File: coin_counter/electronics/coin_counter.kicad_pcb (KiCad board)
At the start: 2 copper layers, 185.3 x 82 mm, 54 parts, among them J1 Q_EMT, J10 H_EMT, J11 Power In, J12 Q_BTN, J13 D_BTN, J14 N_BTN, J15 P_BTN, J16 UP_BTN, J17 DN_BTN, J18 VFD, J19 i/o in, J2 N_EMT, J20 i/o in, J21 Power In, J22 Power Out, J23 i/o out, J24 i/o out, J25 H_RCV, J3 P_EMT, J4 D_EMT, J5 Mom, J6 D_RCV, J7 P_RCV, J8 N_RCV, J9 Q_RCV, U1 74HC595, U2 74HC165, U3 74HC165

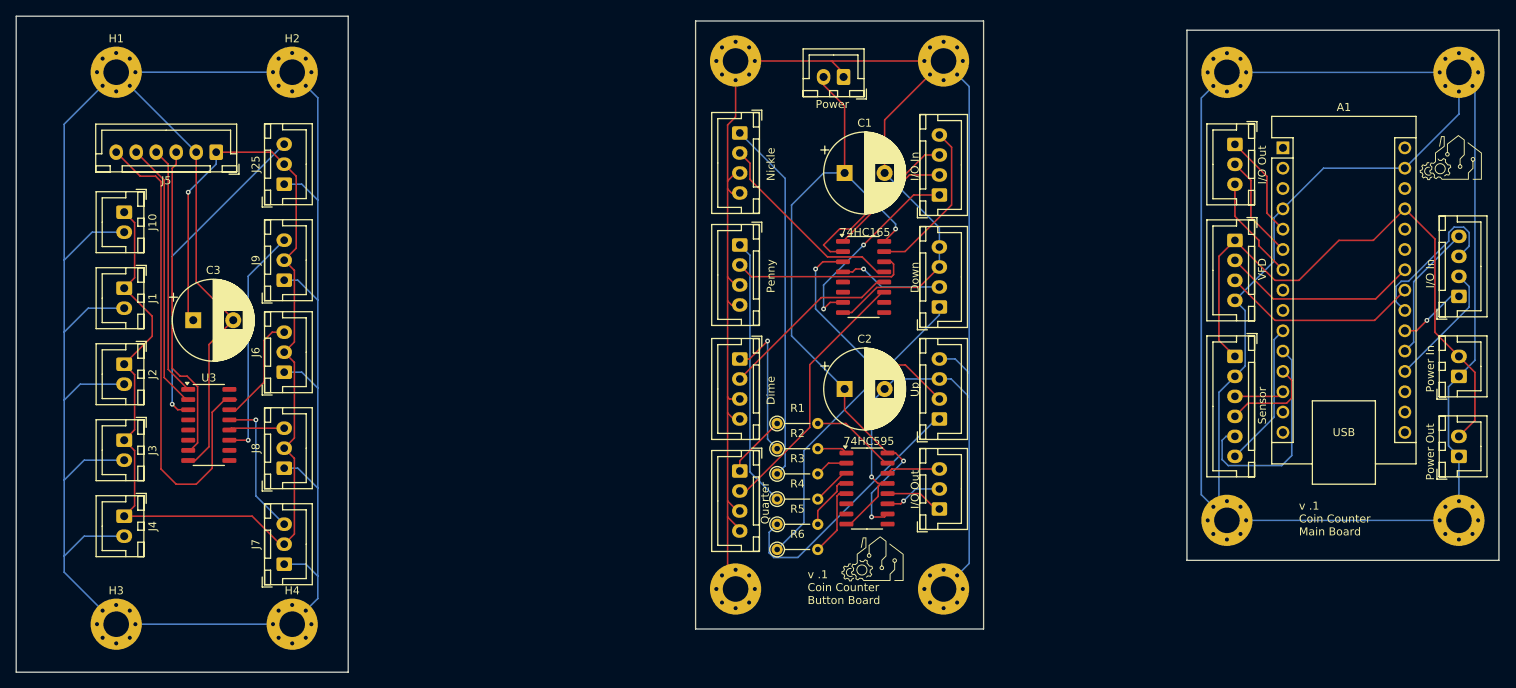
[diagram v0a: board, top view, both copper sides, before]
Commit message: more work, mosfets and diodes
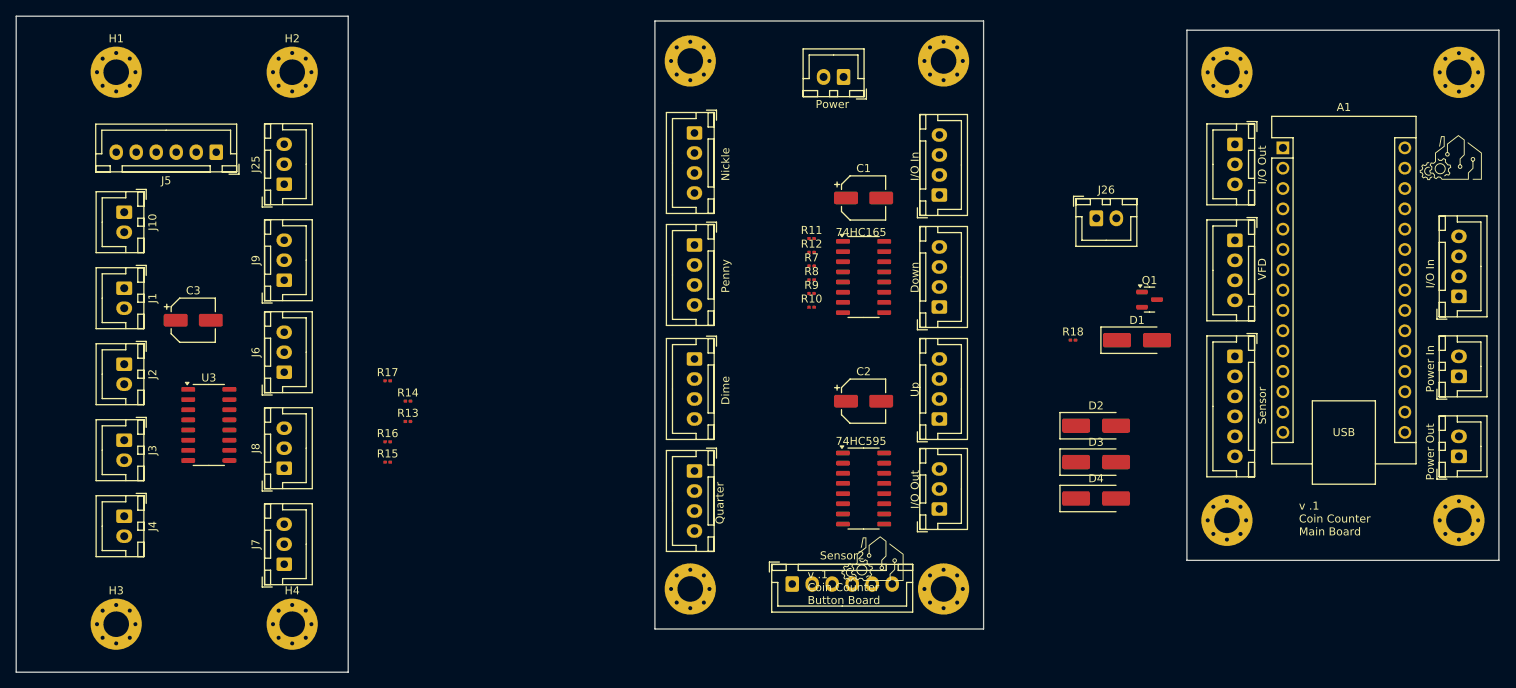
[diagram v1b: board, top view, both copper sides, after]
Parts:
- removed R1, R2, R3, R4, R5, R6: 220 Ohm, Resistor_THT:R_Axial_DIN0204_L3.6mm_D1.6mm_P5.08mm_Vertical
- added D1: D_Schottky, Diode_SMD:D_SMA_Handsoldering, F.Cu at (162.6, 63.5)
- added D2: D_Schottky, Diode_SMD:D_SMA_Handsoldering, F.Cu at (157.5, 74.2)
- added D3: D_Schottky, Diode_SMD:D_SMA_Handsoldering, F.Cu at (157.5, 78.7)
- added D4: D_Schottky, Diode_SMD:D_SMA_Handsoldering, F.Cu at (157.5, 83.3)
- added J26: Motor, Connector_JST:JST_XH_B2B-XH-A_1x02_P2.50mm_Vertical, F.Cu at (157.5, 48.3)
- added Q1: DMN6075S, Package_TO_SOT_SMD:SOT-23, F.Cu at (164.2, 58.4)
- added R10: 10k, Resistor_SMD:R_0201_0603Metric, F.Cu at (121.9, 59.4)
- added R11: 10k, Resistor_SMD:R_0201_0603Metric, F.Cu at (121.9, 50.8)
- added R12: 10k, Resistor_SMD:R_0201_0603Metric, F.Cu at (121.9, 52.5)
- added R13: 10k, Resistor_SMD:R_0201_0603Metric, F.Cu at (71.5, 73.7)
- added R14: 10k, Resistor_SMD:R_0201_0603Metric, F.Cu at (71.5, 71.1)
- added R15: 10k, Resistor_SMD:R_0201_0603Metric, F.Cu at (68.9, 78.7)
- added R16: 10k, Resistor_SMD:R_0201_0603Metric, F.Cu at (68.9, 76.2)
- added R17: 10k, Resistor_SMD:R_0201_0603Metric, F.Cu at (68.9, 68.6)
- added R18: 10k, Resistor_SMD:R_0201_0603Metric, F.Cu at (154.6, 63.5)
- added R7: 10k, Resistor_SMD:R_0201_0603Metric, F.Cu at (121.9, 54.2)
- added R8: 10k, Resistor_SMD:R_0201_0603Metric, F.Cu at (121.9, 55.9)
- added R9: 10k, Resistor_SMD:R_0201_0603Metric, F.Cu at (121.9, 57.7)
- added Sensor2: Mom, Connector_JST:JST_XH_B6B-XH-A_1x06_P2.50mm_Vertical, F.Cu at (119.5, 94.0)
- C1, C2, C3: footprint Capacitor_THT:CP_Radial_D10.0mm_P5.00mm -> Capacitor_SMD:CP_Elec_5x5.9
- moved J12 5.66 mm to (107.3, 79.8)
- moved J13 5.66 mm to (107.3, 65.8)
- moved J14 5.66 mm to (107.3, 37.6)
- moved J15 5.66 mm to (107.3, 51.6)
- moved H11 5.66 mm to (106.8, 28.6)
- moved H12 5.66 mm to (106.8, 94.6)
- moved C1 3.92 mm to (128.4, 45.7)
- moved C2 2.81 mm to (128.4, 71.1)
- moved U1 0.42 mm to (128.4, 82.0)
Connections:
- A1 pad 10: Net-(A1-D7) -> unconnected-(A1-D7-Pad10)
- A1 pad 11: Net-(A1-D8) -> unconnected-(A1-D8-Pad11)
- A1 pad 12: Net-(A1-D9) -> unconnected-(A1-D9-Pad12)
- A1 pad 13: Net-(A1-D10) -> unconnected-(A1-D10-Pad13)
- A1 pad 29: Net-(J11-Pin_1) -> Net-(D4-A)
- A1 pad 4: Net-(J11-Pin_1) -> Net-(D4-A)
- A1 pad 9: unconnected-(A1-D6-Pad9) -> Net-(A1-D6)
- C1 pad 1: Net-(J21-Pin_2) -> Net-(J12-Pin_3)
- C1 pad 2: Net-(J12-Pin_3) -> Net-(J12-Pin_4)
- C2 pad 1: Net-(J21-Pin_2) -> Net-(J12-Pin_3)
- C2 pad 2: Net-(J12-Pin_3) -> Net-(J12-Pin_4)
- H10 pad 1: Net-(J12-Pin_3) -> Net-(J12-Pin_4)
- H11 pad 1: Net-(J12-Pin_3) -> Net-(J12-Pin_4)
- H12 pad 1: Net-(J12-Pin_3) -> Net-(J12-Pin_4)
- H5 pad 1: Net-(J11-Pin_1) -> Net-(D4-A)
- H6 pad 1: Net-(J11-Pin_1) -> Net-(D4-A)
- H7 pad 1: Net-(J11-Pin_1) -> Net-(D4-A)
- H8 pad 1: Net-(J11-Pin_1) -> Net-(D4-A)
- H9 pad 1: Net-(J12-Pin_3) -> Net-(J12-Pin_4)
- J12 pad 4: Net-(J12-Pin_3) -> Net-(J12-Pin_4)
- J13 pad 4: Net-(J12-Pin_3) -> Net-(J12-Pin_4)
- J14 pad 4: Net-(J12-Pin_3) -> Net-(J12-Pin_4)
- J15 pad 4: Net-(J12-Pin_3) -> Net-(J12-Pin_4)
- J16 pad 4: Net-(J12-Pin_3) -> Net-(J12-Pin_4)
- J17 pad 4: Net-(J12-Pin_3) -> Net-(J12-Pin_4)
- J18 pad 4: Net-(J11-Pin_1) -> Net-(D4-A)
- J21 pad 1: Net-(J12-Pin_3) -> Net-(J12-Pin_4)
- J21 pad 2: Net-(J21-Pin_2) -> Net-(J12-Pin_3)
- U1 pad 1: Net-(U1-QB) -> Net-(J13-Pin_1)
- U1 pad 10: Net-(J21-Pin_2) -> Net-(J12-Pin_3)
- U1 pad 13: Net-(J12-Pin_3) -> Net-(J12-Pin_4)
- U1 pad 15: Net-(U1-QA) -> Net-(J12-Pin_1)
- U1 pad 16: Net-(J21-Pin_2) -> Net-(J12-Pin_3)
- U1 pad 2: Net-(U1-QC) -> Net-(J14-Pin_1)
- U1 pad 3: Net-(U1-QD) -> Net-(J15-Pin_1)
- U1 pad 4: Net-(U1-QE) -> Net-(J16-Pin_1)
- U1 pad 5: Net-(U1-QF) -> Net-(J17-Pin_1)
- U1 pad 8: Net-(J12-Pin_3) -> Net-(J12-Pin_4)
- U2 pad 10: unconnected-(U2-DS-Pad10) -> Net-(Sensor2-Pin_3)
- U2 pad 11: Net-(J12-Pin_2) -> Net-(U2-D0)
- U2 pad 12: Net-(J13-Pin_2) -> Net-(U2-D1)
- U2 pad 13: Net-(J14-Pin_2) -> Net-(U2-D2)
- U2 pad 14: Net-(J15-Pin_2) -> Net-(U2-D3)
- U2 pad 16: Net-(J21-Pin_2) -> Net-(J12-Pin_3)
- U2 pad 3: Net-(J16-Pin_2) -> Net-(U2-D4)
- U2 pad 4: Net-(J17-Pin_2) -> Net-(U2-D5)
- U2 pad 5: unconnected-(U2-D6-Pad5) -> Net-(J12-Pin_4)
- U2 pad 6: unconnected-(U2-D7-Pad6) -> Net-(J12-Pin_4)
- U2 pad 7: Net-(J19-Pin_1) -> unconnected-(U2-~{Q7}-Pad7)
- U2 pad 8: Net-(J12-Pin_3) -> Net-(J12-Pin_4)
- U2 pad 9: unconnected-(U2-Q7-Pad9) -> Net-(J19-Pin_1)
- U3 pad 11: Net-(J9-Pin_3) -> Net-(U3-D0)
- U3 pad 12: Net-(J8-Pin_3) -> Net-(U3-D1)
- U3 pad 13: Net-(J7-Pin_3) -> Net-(U3-D2)
- U3 pad 14: Net-(J6-Pin_3) -> Net-(U3-D3)
- U3 pad 3: Net-(J25-Pin_3) -> Net-(U3-D4)
- U3 pad 7: Net-(J5-Pin_3) -> unconnected-(U3-~{Q7}-Pad7)
- U3 pad 9: unconnected-(U3-Q7-Pad9) -> Net-(J5-Pin_3)
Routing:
- net GND: track 315.9 -> 0.00 mm
- net Net-(J12-Pin_3): track 266.8 -> 0.00 mm, vias 1 -> 0
- net Net-(J11-Pin_1): track 251.2 -> 0.00 mm
- net +5V: track 149.3 -> 0.00 mm, vias 1 -> 0
- net Net-(J21-Pin_2): track 82.4 -> 0.00 mm, vias 3 -> 0
- net Net-(A1-+5V): track 76.1 -> 0.00 mm
- net Net-(J5-Pin_6): track 61.7 -> 0.00 mm
- net Net-(J14-Pin_1): track 45.4 -> 0.00 mm
- net Net-(J25-Pin_3): track 40.6 -> 0.00 mm, vias 1 -> 0
- net Net-(J5-Pin_3): track 39.9 -> 0.00 mm
- net Net-(J17-Pin_1): track 38.7 -> 0.00 mm
- net Net-(J5-Pin_5): track 33.8 -> 0.00 mm
- net Net-(J15-Pin_1): track 33.7 -> 0.00 mm
- net Net-(J12-Pin_2): track 32.9 -> 0.00 mm
- net Net-(J16-Pin_1): track 32.7 -> 0.00 mm
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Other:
- outline, holes or cut-outs redrawn

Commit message: board layouts button and main
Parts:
- removed Sensor: Board, PCM_kikit:Board
- removed Sensor1: Mom, Connector_JST:JST_XH_B6B-XH-A_1x06_P2.50mm_Vertical
- moved D2 47.4 mm to (192.0, 41.8)
- moved D3 46.9 mm to (192.0, 47.0), turned to 180 degrees
- moved D1 39.9 mm to (192.0, 36.5), turned to 180 degrees
- moved D4 38.1 mm to (174.0, 49.0)
- moved R7 31.1 mm to (114.7, 84.5), turned to 180 degrees
- moved J18 31.0 mm to (174.5, 82.0)
- moved J23 31.0 mm to (174.5, 70.0)
- moved R18 30.6 mm to (180.3, 47.0), turned to -90 degrees
- moved J26 20.8 mm to (174.5, 60.2), turned to -90 degrees
- moved R11 20.2 mm to (129.7, 69.5)
- moved R12 16.9 mm to (129.7, 67.5)
- moved R8 16.7 mm to (114.7, 71.0), turned to 180 degrees
- moved A1 15.0 mm to (180.8, 54.5)
- moved R9 13.7 mm to (114.7, 46.0), turned to 180 degrees
- moved H8 12.0 mm to (203.4, 98.0)
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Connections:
- A1 pad 29: Net-(D4-A) -> Net-(J11-Pin_1)
- A1 pad 4: Net-(D4-A) -> Net-(J11-Pin_1)
- D3 pad 1: Net-(D3-K) -> Net-(A1-+5V)
- H5 pad 1: Net-(D4-A) -> Net-(J11-Pin_1)
- H6 pad 1: Net-(D4-A) -> Net-(J11-Pin_1)
- H7 pad 1: Net-(D4-A) -> Net-(J11-Pin_1)
- H8 pad 1: Net-(D4-A) -> Net-(J11-Pin_1)
- J18 pad 4: Net-(D4-A) -> Net-(J11-Pin_1)
- Q1 pad 2: Net-(D4-A) -> Net-(J11-Pin_1)
- Q1 pad 3: Net-(D3-K) -> Net-(D4-A)
- R18 pad 2: Net-(D4-A) -> Net-(J11-Pin_1)
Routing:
- net Net-(J12-Pin_4): track 0.00 -> 298.1 mm
- net Net-(J11-Pin_1): track 0.00 -> 212.4 mm, vias 0 -> 2
- net Net-(J12-Pin_3): track 0.00 -> 169.1 mm, vias 0 -> 5
- net Net-(A1-+5V): track 0.00 -> 120.5 mm
- net Net-(J19-Pin_3): track 0.00 -> 87.6 mm, vias 0 -> 2
- net Net-(J19-Pin_2): track 0.00 -> 82.6 mm, vias 0 -> 3
- net Net-(J19-Pin_4): track 0.00 -> 78.7 mm, vias 0 -> 2
- net Net-(A1-D6): track 0.00 -> 53.8 mm, vias 0 -> 1
- net Net-(A1-SCL/A5): track 0.00 -> 50.1 mm
- net Net-(J14-Pin_1): track 0.00 -> 48.6 mm
- net Net-(Sensor2-Pin_3): track 0.00 -> 47.7 mm, vias 0 -> 1
- net Net-(A1-SDA/A4): track 0.00 -> 46.3 mm
- net Net-(D1-A): track 0.00 -> 40.2 mm
- net Net-(J15-Pin_1): track 0.00 -> 39.0 mm
- net Net-(J17-Pin_1): track 0.00 -> 34.7 mm, vias 0 -> 1
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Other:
- board size 185.3 x 82 mm -> 185.5 x 82 mm
- board text added: "Motor"
- board text added: "v .2 Coin Counter Button Board"
- board text added: "v .2 Coin Counter Main Board"
- board text removed: "Sensor"
- board text removed: "v .1 Coin Counter Button Board"
- board text removed: "v .1 Coin Counter Main Board"

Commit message: v2 of boards
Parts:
- added Sensor_2: Board, PCM_kikit:Board, F.Cu at (44.0, 25.5)
- moved H5 56.4 mm to (118.7, 28.6)
- moved A1 56.4 mm to (125.3, 44.6)
- moved D1 56.4 mm to (136.5, 26.6)
- moved D2 56.4 mm to (136.5, 31.9)
- moved D3 56.4 mm to (136.5, 37.1)
- moved D4 56.4 mm to (118.5, 39.1)
- moved H7 56.4 mm to (148.5, 28.6)
- moved J20 56.4 mm to (146.5, 59.6)
- moved J23 56.4 mm to (119.0, 60.1)
- moved J26 56.4 mm to (119.0, 50.4)
- moved Main 56.4 mm to (121.5, 23.1)
- moved Q1 56.4 mm to (118.5, 44.1)
- moved R18 56.4 mm to (124.8, 37.1)
- moved H8 56.4 mm to (147.9, 88.2)
- moved J11 56.4 mm to (146.5, 69.7)
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- renumbered U3 to 74HC165, J4 to D_EMT, J6 to D_RECV, J10 to H_EMT, J25 to H_RECV, J2 to N_EMT, J8 to N_RECV, J3 to P_EMT, J7 to P_RECV, J9 to Q_RECV, J5 to Sensor
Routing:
- net GND: track 0.00 -> 282.2 mm
- net +5V: track 0.00 -> 173.6 mm, vias 0 -> 2
- net Net-(J5-Pin_6): track 0.00 -> 54.7 mm, vias 0 -> 1
- net Net-(J5-Pin_4): track 0.00 -> 47.0 mm, vias 0 -> 2
- net Net-(J5-Pin_5): track 0.00 -> 42.2 mm, vias 0 -> 1
- net Net-(J5-Pin_3): track 0.00 -> 40.0 mm, vias 0 -> 2
- net Net-(U3-D4): track 0.00 -> 36.1 mm
- net Net-(U3-D0): track 0.00 -> 35.6 mm
- net Net-(U3-D3): track 0.00 -> 20.6 mm
- net Net-(U3-D1): track 0.00 -> 16.7 mm, vias 0 -> 2
- net Net-(U3-D2): track 0.00 -> 10.1 mm
- net Net-(J8-Pin_3): track 0.00 -> 6.67 mm
- net Net-(J9-Pin_3): track 0.00 -> 4.02 mm
- net Net-(J7-Pin_3): track 0.00 -> 4.02 mm
- net Net-(J25-Pin_3): track 0.00 -> 4.02 mm
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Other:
- board size 185.5 x 82 mm -> 122.5 x 80.3 mm
- board text added: "v .2 Coin Counter Sensor Board"

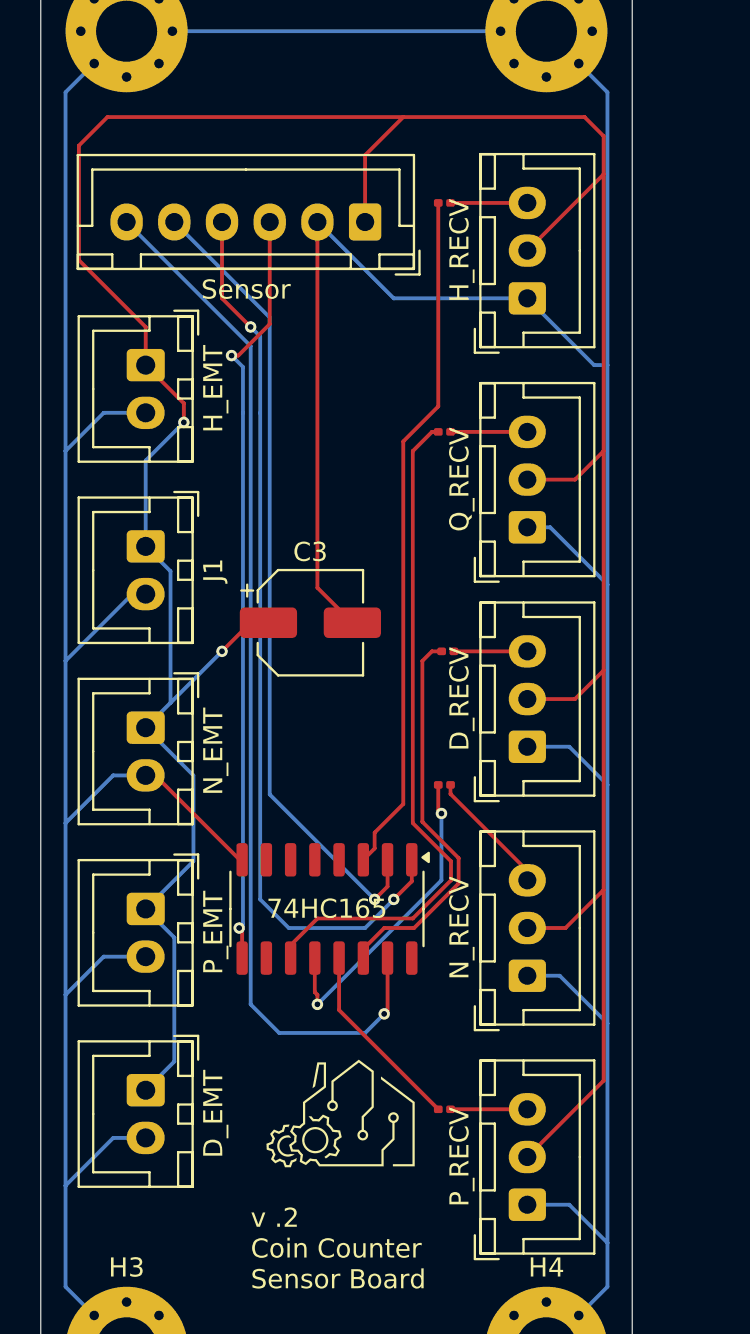
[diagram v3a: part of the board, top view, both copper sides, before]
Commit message: only take the VFD stuff I need
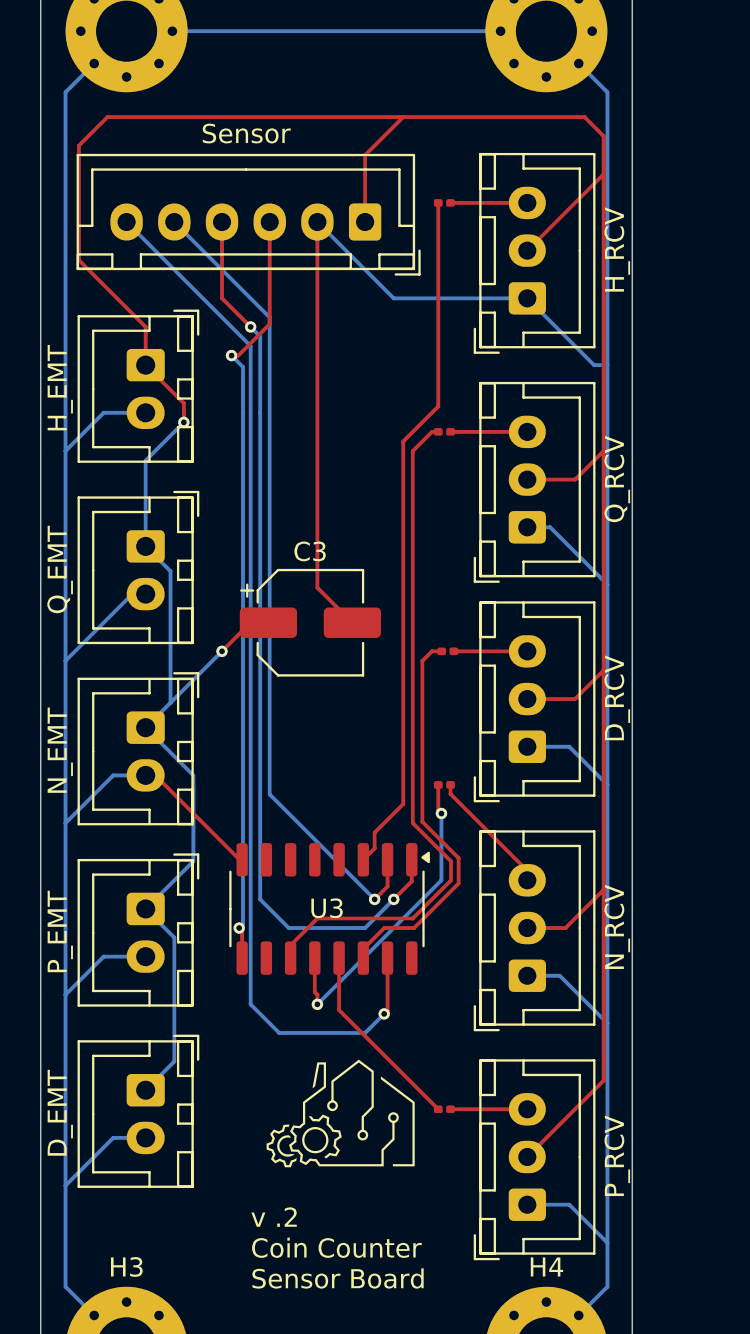
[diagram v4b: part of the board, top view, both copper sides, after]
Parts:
- J5: renamed from Sensor; value Mom -> Sensor
- renumbered H_EMT to J10, N_EMT to J2, H_RECV to J25, P_EMT to J3, D_EMT to J4, D_RECV to J6, P_RECV to J7, N_RECV to J8, Q_RECV to J9, 74HC165 to U3
